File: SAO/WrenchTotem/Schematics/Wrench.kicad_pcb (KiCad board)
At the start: 2 copper layers, 100.4 x 99.6 mm, 19 parts, among them J1 Conn_02x03_Odd_Even, J10 USB_B_Micro, J2 Conn_02x03_Odd_Even, J3 Conn_02x03_Odd_Even, J4 Conn_02x03_Odd_Even, SW1 SW_SPDT, U3 HX4056, U4 TLV1117-33

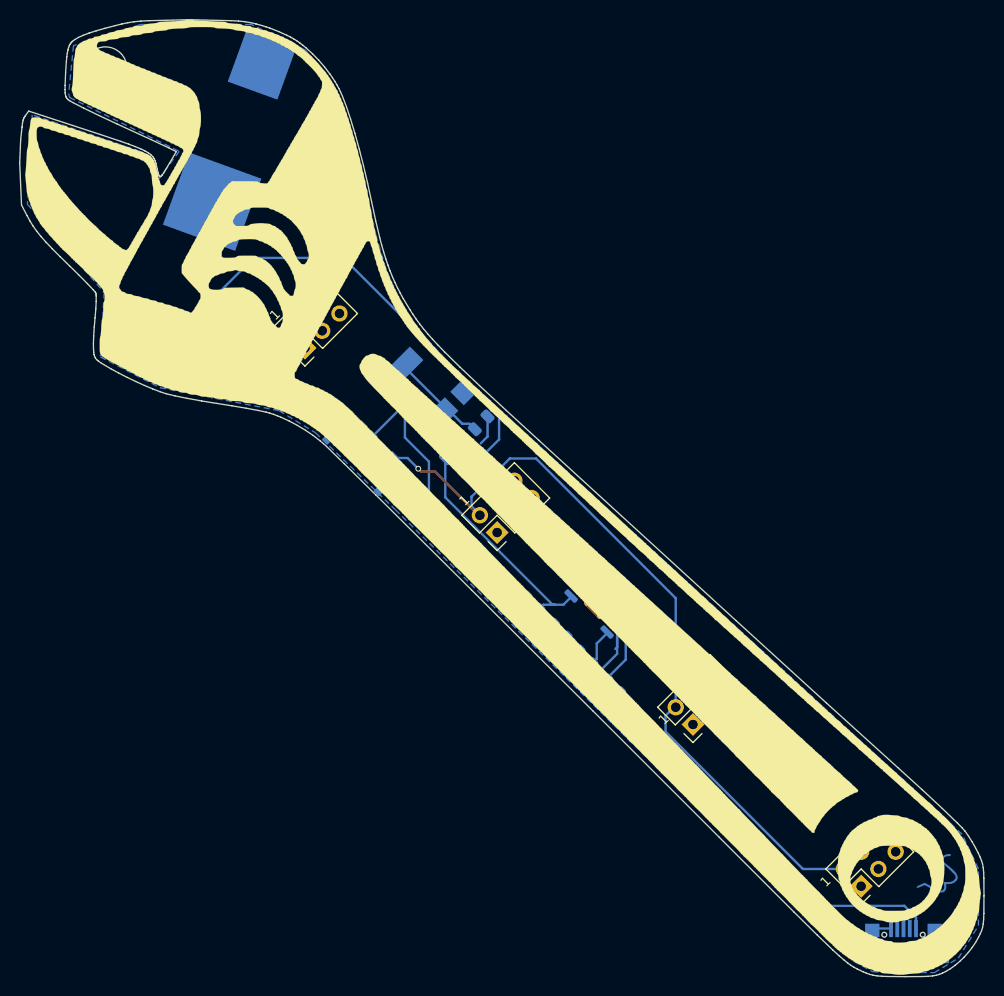
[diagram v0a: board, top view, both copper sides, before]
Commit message: Making stencils
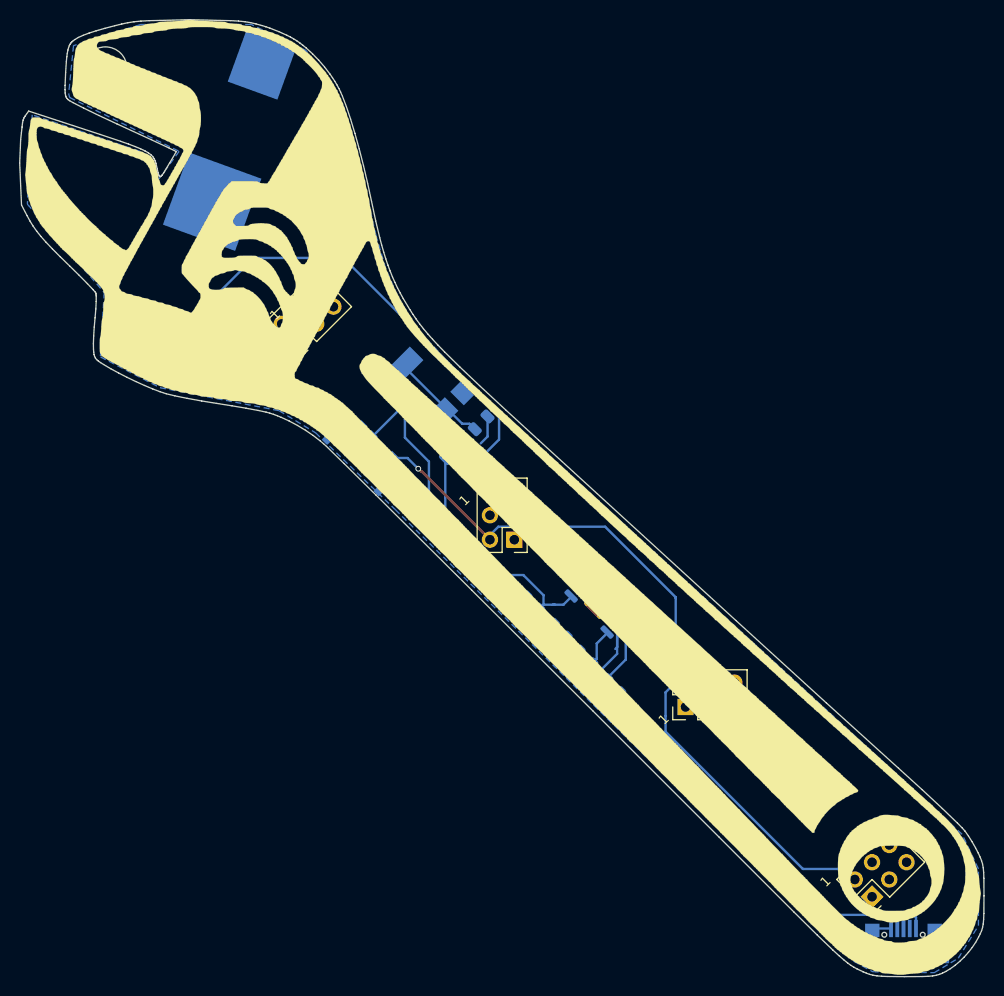
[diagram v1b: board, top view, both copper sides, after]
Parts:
- <- Power: renamed from SW1
- moved Ref** 19.5 mm to (166.8, 126.4), turned to 135 degrees
- moved J4 1.98 mm to (156.7, 117.1), turned to 90 degrees
- moved J2 1.94 mm to (138.9, 99.7), turned to 180 degrees
- moved J1 1.58 mm to (176.1, 136.9)
- moved J3 0.95 mm to (116.5, 79.1)
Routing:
- net VDD: track 101.8 -> 99.4 mm
- net VDDA: track 82.2 -> 83.6 mm
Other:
- board text added: "Made For Defcon 27"
- board text added: "RMA Badge"
